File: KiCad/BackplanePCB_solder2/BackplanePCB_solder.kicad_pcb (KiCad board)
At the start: 2 copper layers, 471 x 73 mm, 84 parts, among them J1 Conn_02x05_Odd_Even, J10 Conn_01x03, J11 Conn_01x03, J12 Conn_01x03, J13 Conn_01x03, J14 Conn_01x03, J15 Conn_01x03, J16 DB15_Female_MountingHoles, J17 DB15_Female_MountingHoles, J18 Conn_01x03, J19 DB15_Female_MountingHoles, J2 Conn_02x05_Odd_Even, J20 DB15_Female_MountingHoles, J21 DB15_Female_MountingHoles, J22 DB15_Female_MountingHoles, J23 DB15_Female_MountingHoles, J24 DB15_Female_MountingHoles, J25 Conn_01x06, J3 PowerBug+15V, J4 PowerBug_GND, J5 Conn_01x03, J6 Conn_01x03, J7 Conn_01x03, J8 DB15_Female_MountingHoles, J9 DB15_Female_MountingHoles, Q1 Q_NMOS_GSD, U1 ST485EBDR, U2 ST485EBDR, U3 ST485EBDR, U4 KA78M05_TO252, U5 ST485EBDR, U6 PIC16F18854-SO

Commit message: new BackplanePCB_solder2/BackplanePCB_solder.kicad_pcb finished. Created a left only version (length < 300mm) for testing.
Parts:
- added REF**: ESD-Logo_13.2x12mm_SilkScreen, Symbol:ESD-Logo_13.2x12mm_SilkScreen, F.Cu at (185.0, 189.0)
- added REF**: KiCad-Logo2_12mm_SilkScreen, Symbol:KiCad-Logo2_12mm_SilkScreen, F.Cu at (376.0, 170.0)
- added REF**: OSHW-Logo2_14.6x12mm_SilkScreen, Symbol:OSHW-Logo2_14.6x12mm_SilkScreen, F.Cu at (276.0, 170.0)
- moved J2 11.0 mm to (469.9, 170.2)
- moved J1 10.8 mm to (71.1, 170.2)
- moved R1 1.91 mm to (45.0, 195.0)
- moved R3 1.82 mm to (45.0, 183.0)
- moved R2 1.82 mm to (45.0, 189.0)
- moved R14 1.05 mm to (177.3, 174.3)
- moved C13 1.02 mm to (231.1, 168.1)
- moved C5 1.02 mm to (229.6, 173.7)
- moved C8 1.02 mm to (231.9, 173.7)
- moved R10 1.02 mm to (231.1, 170.4)
- moved R17 1.02 mm to (231.1, 165.9)
- moved R6 1.02 mm to (227.3, 173.7)
- moved R21 0.25 mm to (196.7, 165.4)
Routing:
- net GND: track 89.0 -> 340.8 mm, vias 14 -> 18
- net ICSPCLK: track 0.00 -> 67.4 mm, vias 0 -> 1
- net ICSPDAT: track 0.00 -> 64.1 mm, vias 0 -> 1
- net RST: track 10.5 -> 70.8 mm, vias 0 -> 2
- net RX_B: track 473.2 -> 525.8 mm, vias 2 -> 4
- net RESET_B: track 457.6 -> 507.2 mm, vias 0 -> 4
- net TX_B: track 469.0 -> 518.1 mm, vias 2 -> 4
- net RX_A: track 475.6 -> 519.4 mm, vias 2 -> 4
- net SYNC_B: track 479.8 -> 521.5 mm, vias 2 -> 4
- net RESET_A: track 461.0 -> 502.7 mm, vias 0 -> 4
- net TX_A: track 469.2 -> 509.4 mm, vias 2 -> 4
- net SYNC_A: track 482.2 -> 515.1 mm, vias 2 -> 4
- net +5V: track 136.4 -> 159.3 mm
- net Net-(R9-Pad1): track 0.00 -> 8.86 mm
- net Net-(C5-Pad1): track 0.00 -> 7.97 mm
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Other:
- board size 471 x 73 mm -> 470 x 59 mm
- board text added: "+15V"
- board text added: "."
- board text added: "0V"
- board text added: "1"
- board text added: "10"
- board text added: "15"
- board text added: "2"
- board text added: "3"
- board text added: "4"
- board text added: "5"
- board text added: "6"
- board text added: "7"
- board text added: "8"
- board text added: "9"
- board text added: ">"
- board text added: "ID"
- board text added: "ID_1"
- board text added: "JSIF 2018"
- board text added: "RESET"
- board text added: "RESET_A"
- board text added: "RESET_B"
- board text added: "RS485 BUS IN"
- board text added: "RS485 BUS OUT"
- board text added: "RX_A"
- board text added: "RX_B"
- board text added: "SLAVE"
- board text added: "SYNC"
- board text added: "SYNC_A"
- board text added: "SYNC_B"
- board text added: "TRACK AMPLIFIER BACKPLANE"
- board text added: "TX_A"
- board text added: "TX_B"
- board text added: "WITH MODBUS SLAVE"

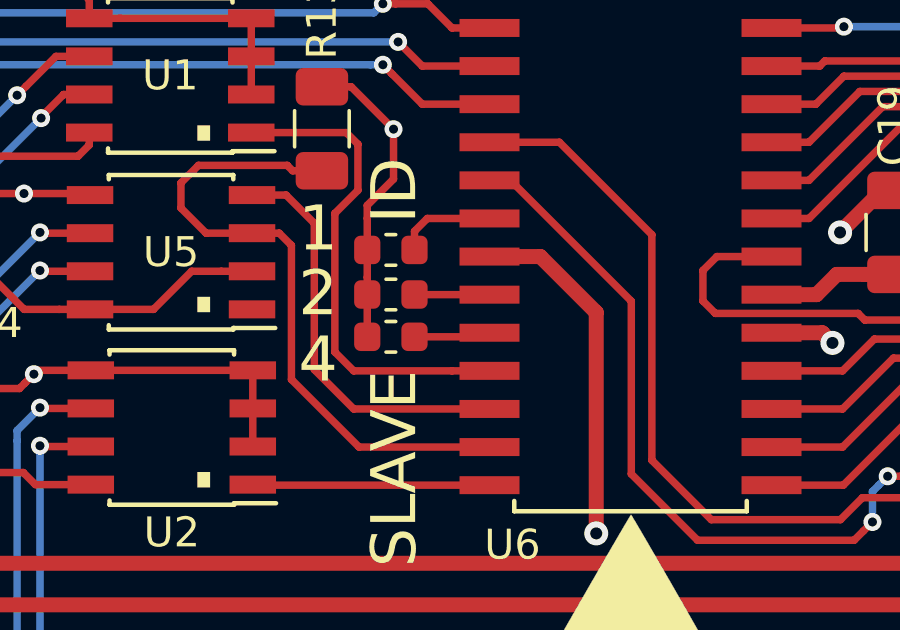
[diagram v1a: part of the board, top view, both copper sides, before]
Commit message: Updating design according to findings on proto (LEFT  config). Still some spces between sub -d screws is NOK.
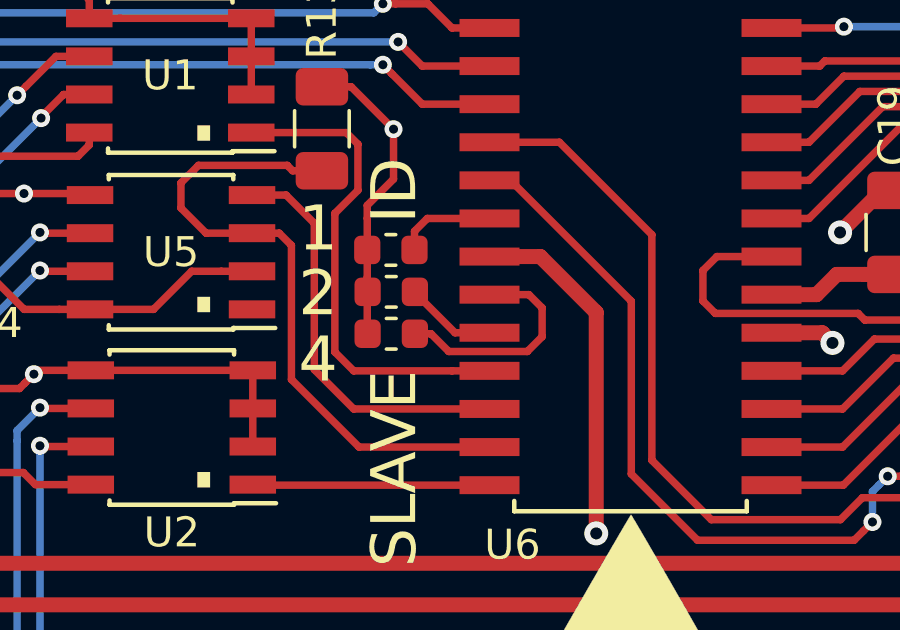
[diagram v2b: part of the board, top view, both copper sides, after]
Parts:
- moved R15 1.50 mm to (177.3, 175.7)
- moved R16 1.31 mm to (177.3, 177.1)
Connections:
- J16 pad 7: ID_2 -> ID_9
- J17 pad 7: ID_7 -> ID_4
- J19 pad 7: ID_3 -> ID_8
- J20 pad 7: ID_8 -> ID_3
- J21 pad 7: ID_4 -> ID_7
- J22 pad 7: ID_9 -> ID_2
- J23 pad 7: ID_5 -> ID_6
- J24 pad 7: ID_10 -> ID_1
- J8 pad 7: ID_1 -> ID_10
- J9 pad 7: ID_6 -> ID_5
- U6 pad 15: ID_6 -> ID_5
- U6 pad 16: ID_7 -> ID_4
- U6 pad 17: ID_8 -> ID_3
- U6 pad 18: ID_9 -> ID_2
- U6 pad 2: ID_1 -> ID_10
- U6 pad 21: ID_10 -> ID_1
- U6 pad 3: ID_2 -> ID_9
- U6 pad 4: ID_3 -> ID_8
- U6 pad 5: ID_4 -> ID_7
- U6 pad 6: ID_5 -> ID_6
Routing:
- net ID_10: track 318.8 -> 138.3 mm, vias 0 -> 2
- net ID_1: track 138.3 -> 318.8 mm, vias 2 -> 0
- net ID_9: track 263.0 -> 88.0 mm, vias 0 -> 2
- net ID_2: track 88.0 -> 263.0 mm, vias 2 -> 0
- net ID_8: track 213.0 -> 52.8 mm, vias 0 -> 1
- net ID_3: track 52.8 -> 213.0 mm, vias 1 -> 0
- net ID_7: track 163.0 -> 29.7 mm
- net ID_4: track 29.7 -> 163.0 mm
- net ID_6: track 113.0 -> 79.9 mm, vias 0 -> 2
- net ID_5: track 79.9 -> 113.0 mm, vias 2 -> 0
- net Net-(R16-Pad1): track 2.50 -> 7.59 mm
- net Net-(R15-Pad1): track 2.56 -> 3.07 mm
